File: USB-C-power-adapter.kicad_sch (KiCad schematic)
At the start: 65 parts, among them J1 USB-C_GCT_USB4105-GF-A, J2 JST_SH_1x4_SM04B-SRSS-TB-LF-SN, J3 Conn_Molex_NanoFit_1053131202, Q1 SQS401EN-T1_BE3, U1 TPD4E02B04DQA, U2 SIC477ED-T1-GE3, U3 STUSB4500_QFN, U4 TPD4E02B04DQA

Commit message: [#57006] Update connections
Change nanofit connector
Change feedback resistors to 0.1%
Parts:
- removed J3: Conn_Molex_NanoFit_1053131202, thunderbolt-gpu-adapter-footprints:Conn_Molex_NanoFit_1053131202, symbol thunderbolt-gpu-adapter:Conn_Molex_NanoFit_1053131202
- removed R14: R_10k_0402, antmicro-footprints:R_0402_1005Metric, symbol antmicroResistors0402:R_10k_0402
- removed R15: R_140k_0402, antmicro-footprints:R_0402_1005Metric, symbol antmicroResistors0402:R_140k_0402
- removed TP1, TP2, TP3: TP_1.5mm_SMD, antmicro-footprints:TP_SMD_1.5mm, symbol antmicroTestPoints:TP_1.5mm_SMD
- added J4: Molex_Nano-Fit_1x2_105313-2202_Horizontal, antmicro-footprints:Conn_Molex_Nano-Fit_1x2_105313-2202_Horizontal, symbol antmicroWire2BoardConnectors:Molex_Nano-Fit_1x2_105313-2202_Horizontal
- added R13: R_140k_0.1%_0402, antmicro-footprints:R_0402_1005Metric, symbol antmicroResistors0402:R_140k_0.1%_0402
- added R14: R_10k_0.1%_0402, antmicro-footprints:R_0402_1005Metric, symbol antmicroResistors0402:R_10k_0.1%_0402
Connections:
- net VIN is gone; now on net VCC: FB1.1
- net GND: now also J4.2, R14.1
- net at F2.2: now also J4.1
- net 5V0_SYS renamed 12V0
- net 12V0: now also R13.2
- net 5V_BOOT: no longer names the net of C8.2, U2.4 (BOOT)
- net 5V_COMP: no longer names the net of R12.1, U2.21 (COMP)
- net 5V_EN: no longer names the net of R6.1, U2.3 (EN)
- net 5V_FB: no longer names the net of U2.22 (V_{FB})
- net 5V_FB: now also R13.1, R14.2
- net 5V_FSW renamed 12V_FSW
- net 5V_ILIM renamed 12V_ILIM
- net 5V_MODE renamed 12V_MODE
- net 5V_PHASE: no longer names the net of R10.2, U2.5 (PHASE), U2.6 (PHASE)
- net 5V_SNS renamed 12V_SNS
- net 5V_SS renamed 12V_SS
- net 5V_SW: no longer names the net of L1.1, R11.1, U2.12 (SW), U2.13 (SW), U2.14 (SW)
- net 5V_VIN: no longer names the net of C4.1, C5.1, C7.1, FB1.2, R6.2, U2.1 (V_{CIN}), U2.7 (V_{IN}), U2.8 (V_{IN})
- net VDD_5V_DCDC renamed VDD_12V_DCDC
- net VDRV_5V_DCDC renamed VDRV_12V_DCDC
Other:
- note added: "NanoFit Output Connector"
- note removed: "12A"
- note removed: "1MHz"
- note removed: "TODO add the MOLEX nano fit 1053131202 to the library"
- note removed: "TODO: change to 0.1% resistor ??"
- moved on the sheet: C1, C10, C11, C12, C13, C14, C15, C2, C20, C21, C22, C23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

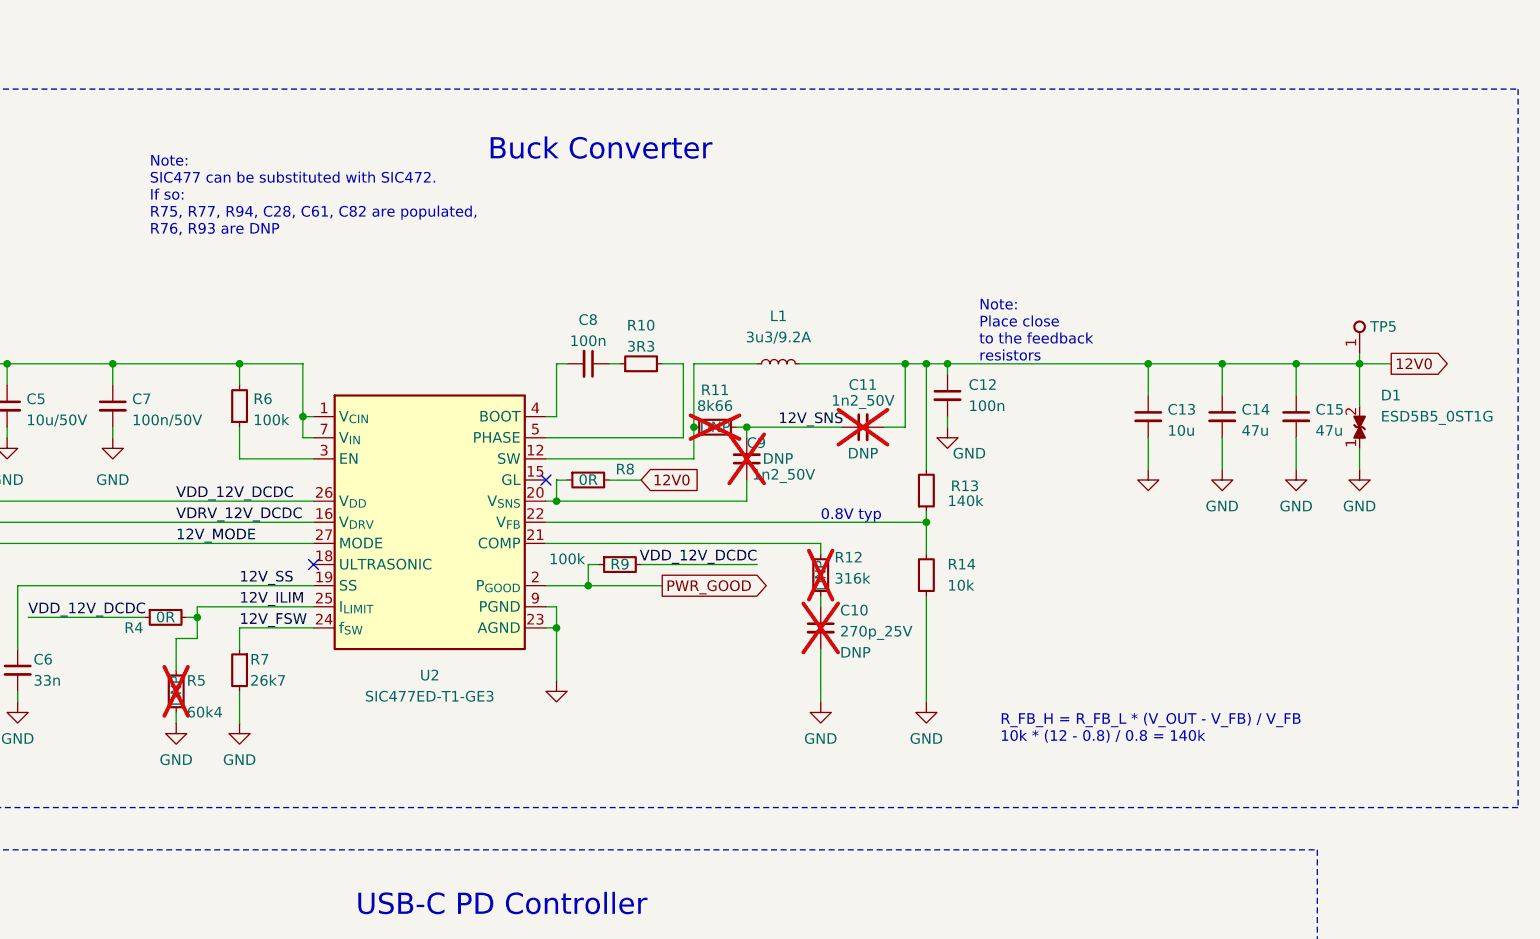
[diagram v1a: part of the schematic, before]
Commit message: [#57006] Change C13, C14, C16
Use capactitors rated for higher voltages
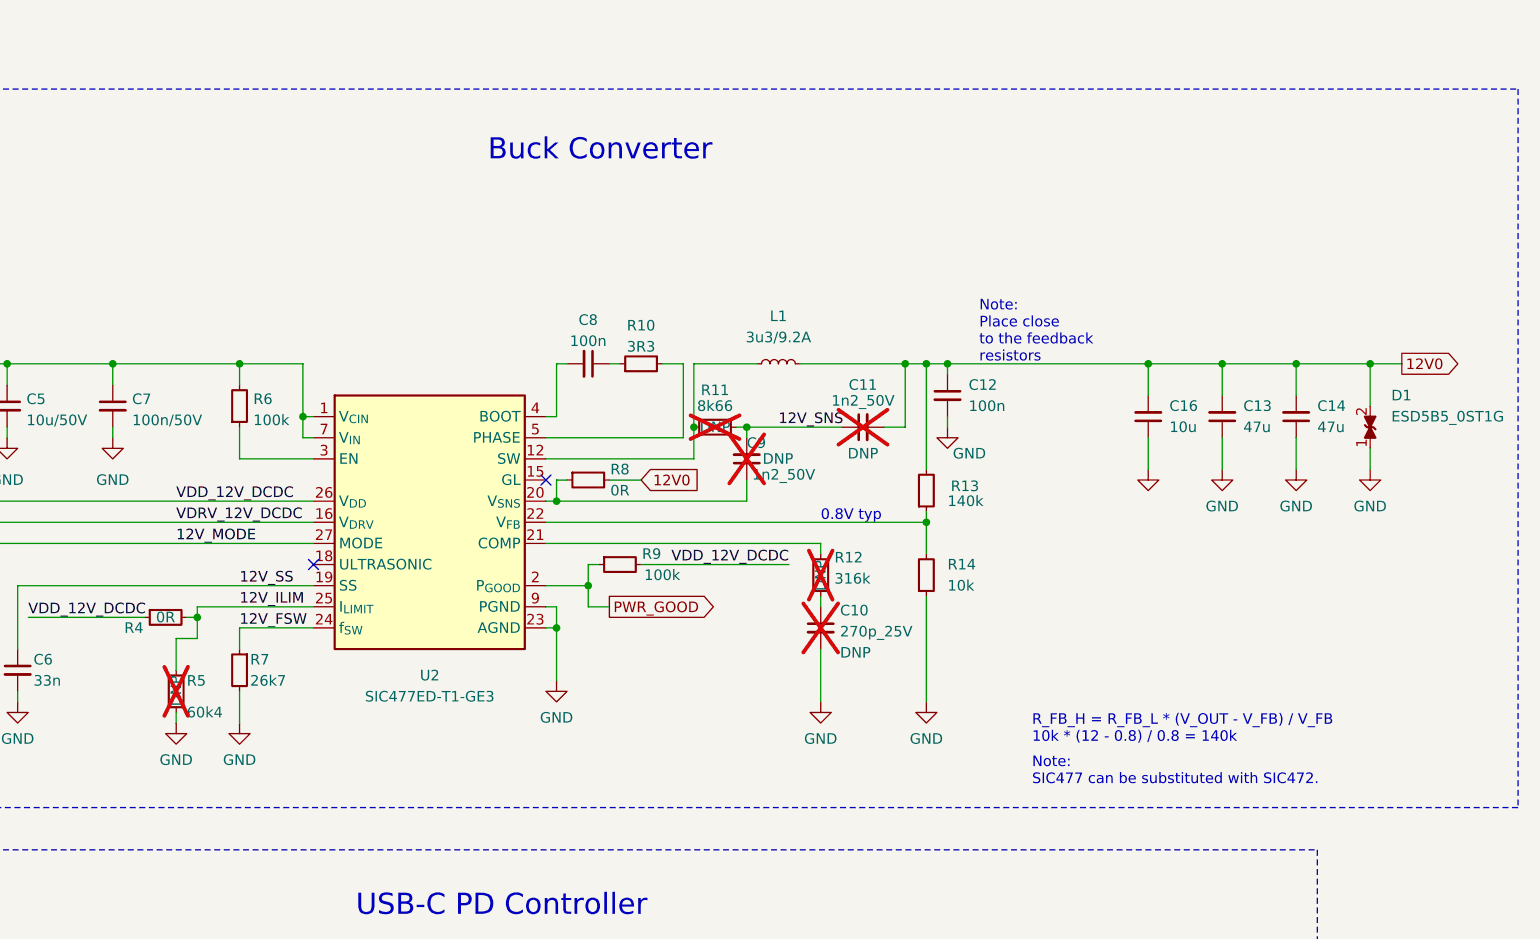
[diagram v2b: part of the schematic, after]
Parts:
- removed C13: C_10u_0603, antmicro-footprints:C_0603_1608Metric, symbol antmicroCapacitors0603:C_10u_0603
- removed C14, C15: C_47u_0805, antmicro-footprints:C_0805_2012Metric, symbol antmicroCapacitorsmisc:C_47u_0805
- removed TP5: TP_1.5mm_SMD, antmicro-footprints:TP_SMD_1.5mm, symbol antmicroTestPoints:TP_1.5mm_SMD
- added C13, C14: C_47u_16V_1206, antmicro-footprints:C_1206_3216Metric, symbol antmicroCapacitorsmisc:C_47u_16V_1206
- added C16: C_10u_25V_0603, antmicro-footprints:C_0603_1608Metric, symbol antmicroCapacitors0603:C_10u_25V_0603
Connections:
- net 12V0: now also C13.2, C14.2, C16.2
- net GND: now also C13.1, C14.1, C16.1
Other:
- note added: "Note: SIC477 can be substituted with SIC472."
- note removed: "Note: SIC477 can be substituted with SIC472. If so: R75, R77, R94, C28, C61, C82 are populated, R76, R93 are DNP"
- moved on the sheet: D1

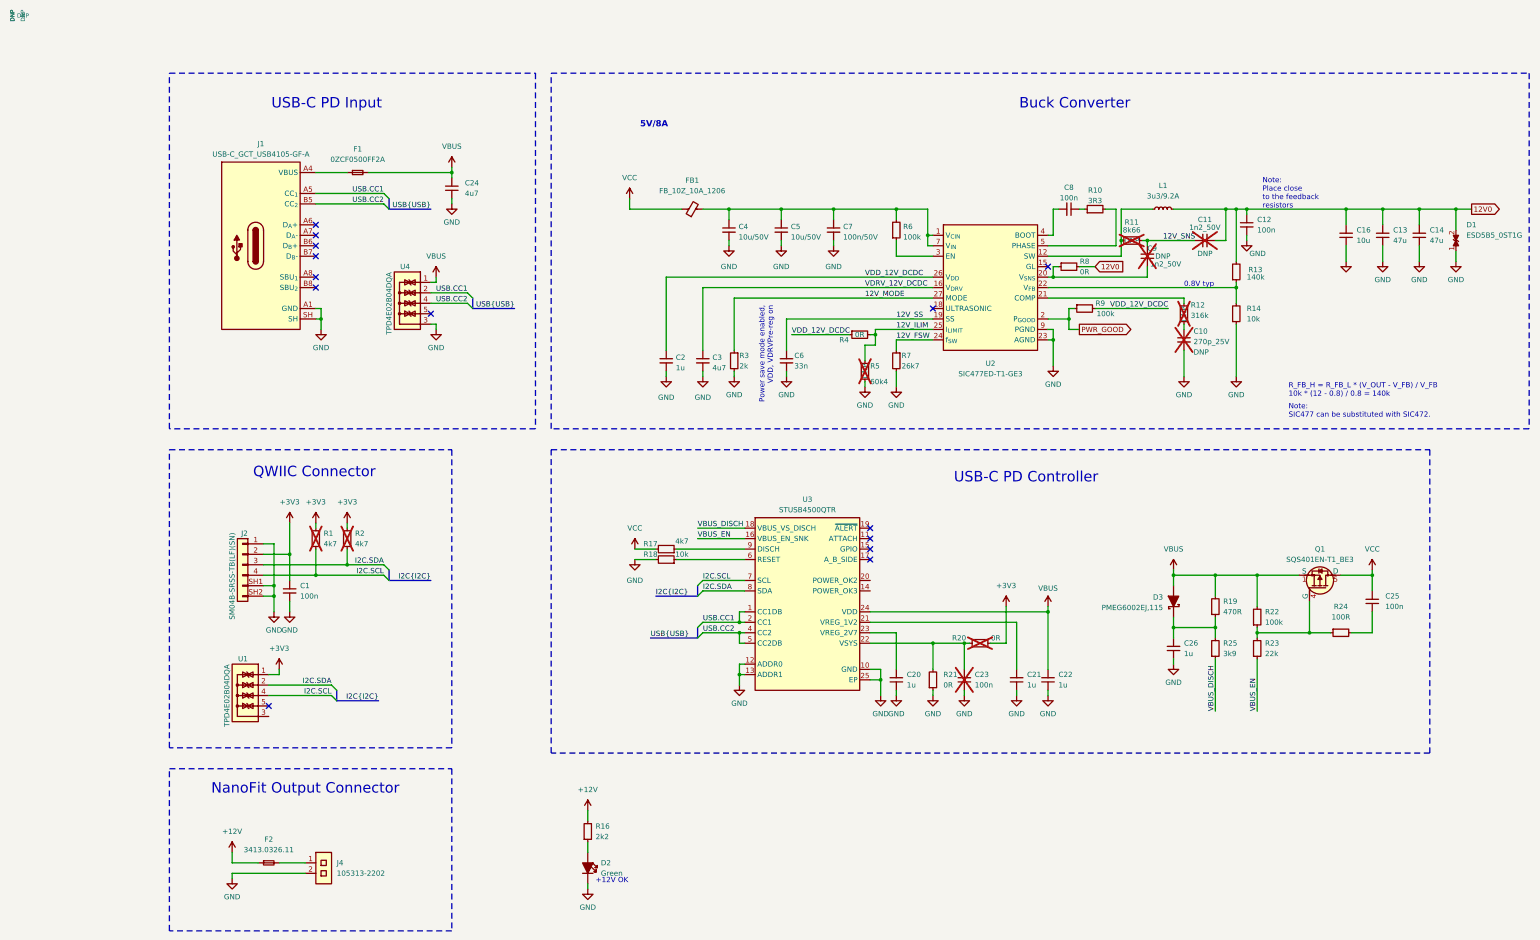
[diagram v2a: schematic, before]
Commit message: [#57006] Add 3v3 and 5v dcdc converters
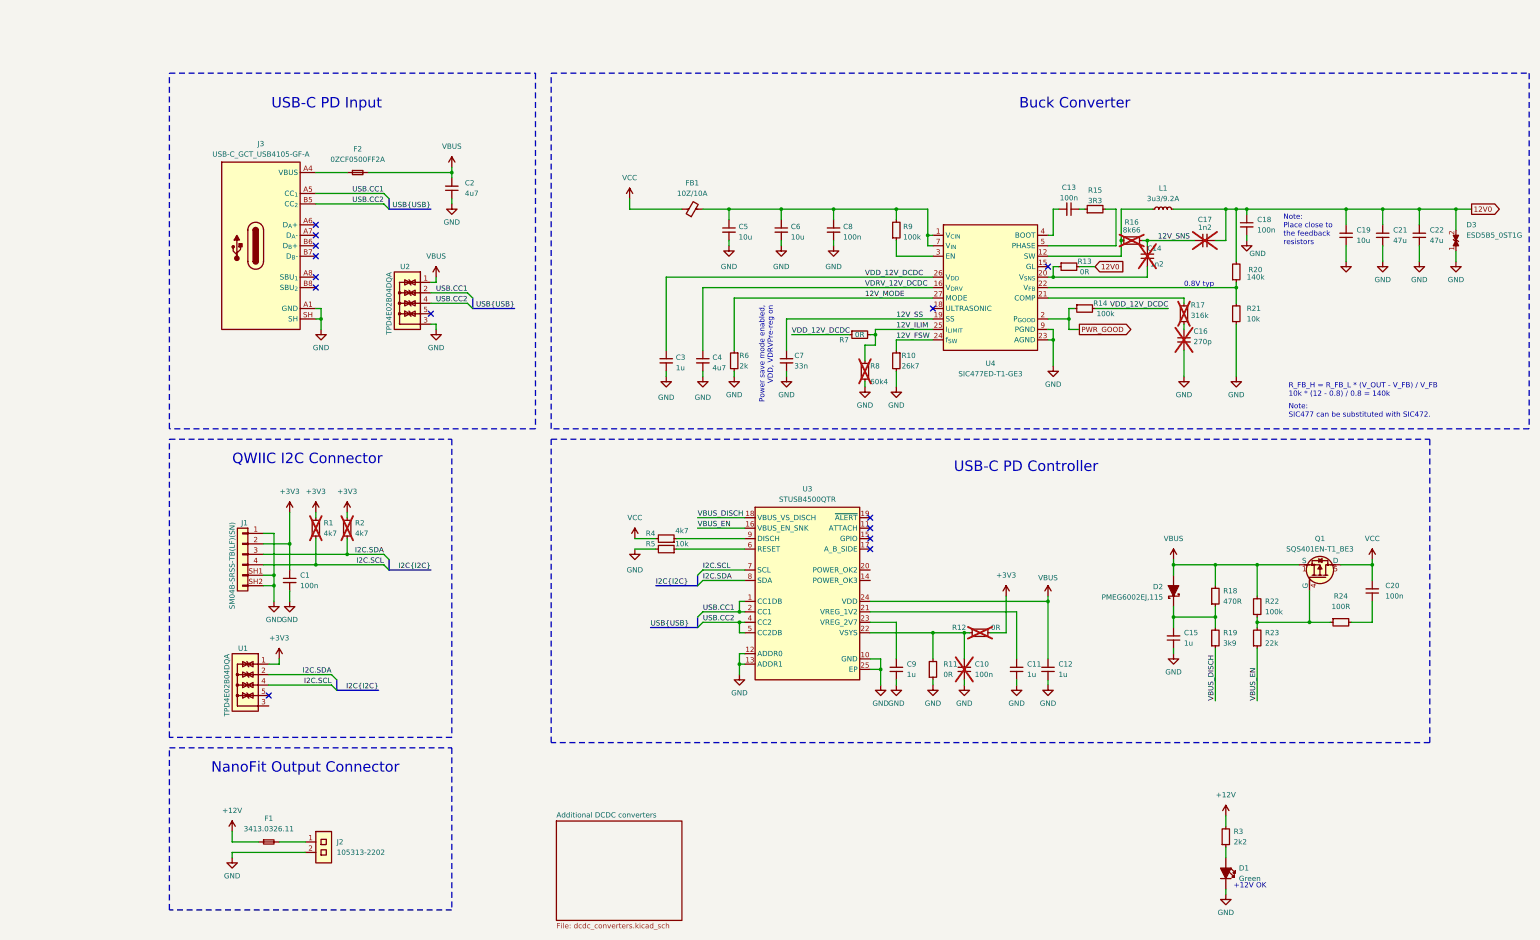
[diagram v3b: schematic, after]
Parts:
- C14: renamed from C9; Val 1n2_50V -> 1n2; Voltage (none) -> 50V
- C16: renamed from C10; Val 270p_25V -> 270p; Voltage (none) -> 25V
- C17: renamed from C11; Val 1n2_50V -> 1n2; Voltage (none) -> 50V
- C5: renamed from C4; Val 10u/50V -> 10u; Voltage (none) -> 50V
- C6: renamed from C5; Val 10u/50V -> 10u; Voltage (none) -> 50V
- C8: renamed from C7; Val 100n/50V -> 100n; Voltage (none) -> 50V
- FB1: value FB_10Z_10A_1206 -> FB_10Z_10A_WE-MPSB_1206; symbol antmicroFerriteBeadsandChips:FB_10Z_10A_1206 -> antmicroFerriteBeadsandChips:FB_10Z_10A_WE-MPSB_1206; Val (none) -> 10Z/10A
- L1: value IHLP3232DZER3R3M01 -> L_3u3_9.2A_Vishay-IHLP-3232DZ-01; footprint antmicro-footprints:L_Vishay_IHLP3232DZ -> antmicro-footprints:L_Vishay-IHLP3232DZ; symbol antmicroFixedInductors:IHLP3232DZER3R3M01 -> antmicroFixedInductors:L_3u3_9.2A_Vishay-IHLP-3232DZ-01; IMax 9.2A -> 9.2 A; ISat 20A -> 20 A
- renumbered C23 to C10, C21 to C11, C22 to C12, C8 to C13, C26 to C15, C12 to C18, C16 to C19, C24 to C2, C25 to C20, C13 to C21, C14 to C22, C2 to C3, C3 to C4, C6 to C7, C20 to C9, D2 to D1, D3 to D2, D1 to D3, F2 to F1, F1 to F2, J2 to J1, J4 to J2, J1 to J3, R7 to R10, R21 to R11, R20 to R12, R8 to R13, R9 to R14, R10 to R15, R11 to R16, R12 to R17, R19 to R18, R25 to R19, R13 to R20, R14 to R21, R16 to R3, R17 to R4, R18 to R5, R3 to R6, R4 to R7, R5 to R8, R6 to R9, U4 to U2, U2 to U4
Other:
- added sheet Additional DCDC converters (dcdc_converters.kicad_sch)
- note added: "QWIIC I2C Connector"
- note removed: "5V/8A"
- note removed: "QWIIC Connector"
- moved on the sheet: C1, C10, C11, C12, C15, C20, C9, D1, D2, F1, J1, J2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
